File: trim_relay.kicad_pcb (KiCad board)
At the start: 2 copper layers, 75 x 71 mm, 46 parts, among them J1 Conn_01x01, J10 Conn_01x01, J11 Conn_01x01, J12 Conn_01x01, J2 Conn_01x01, J3 Conn_01x01, J4 Conn_01x01, J5 Conn_01x01, J6 Conn_01x01, J7 Conn_01x01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

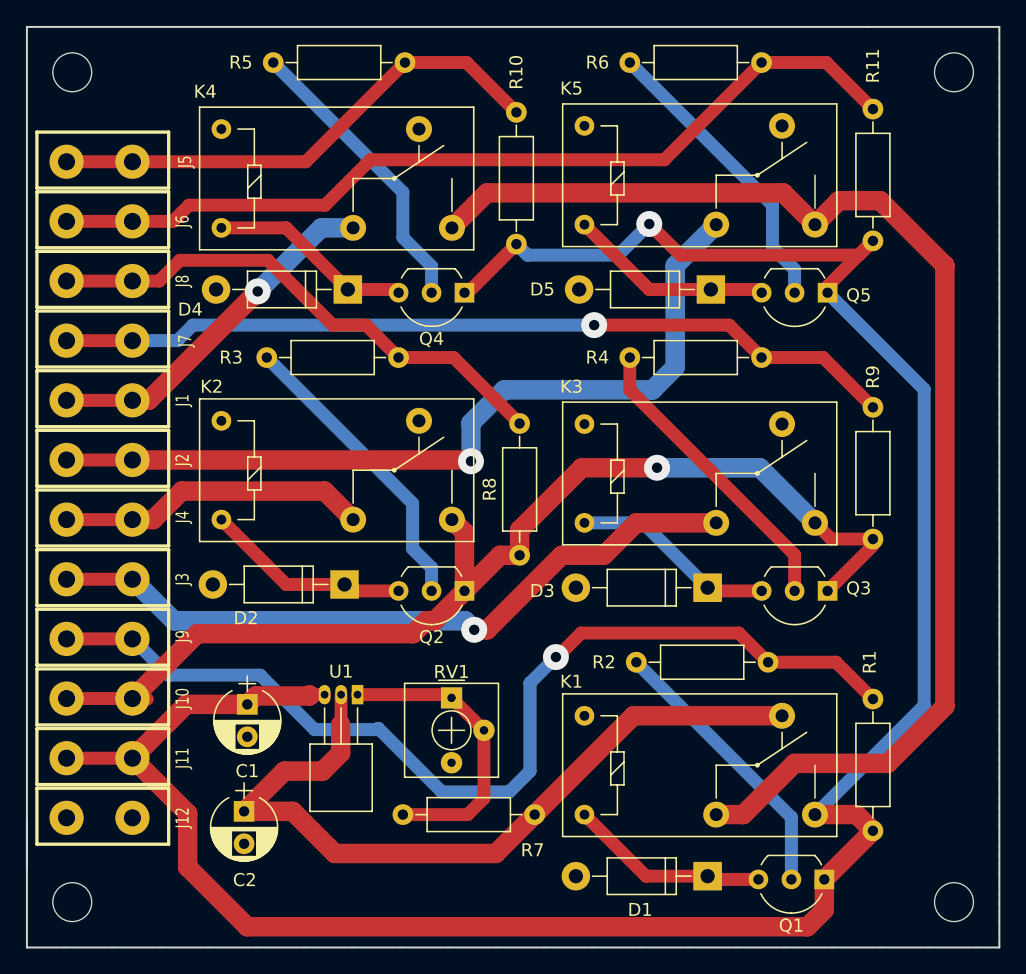
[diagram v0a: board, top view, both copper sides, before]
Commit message: Redid schematic and pcb, removed transistors
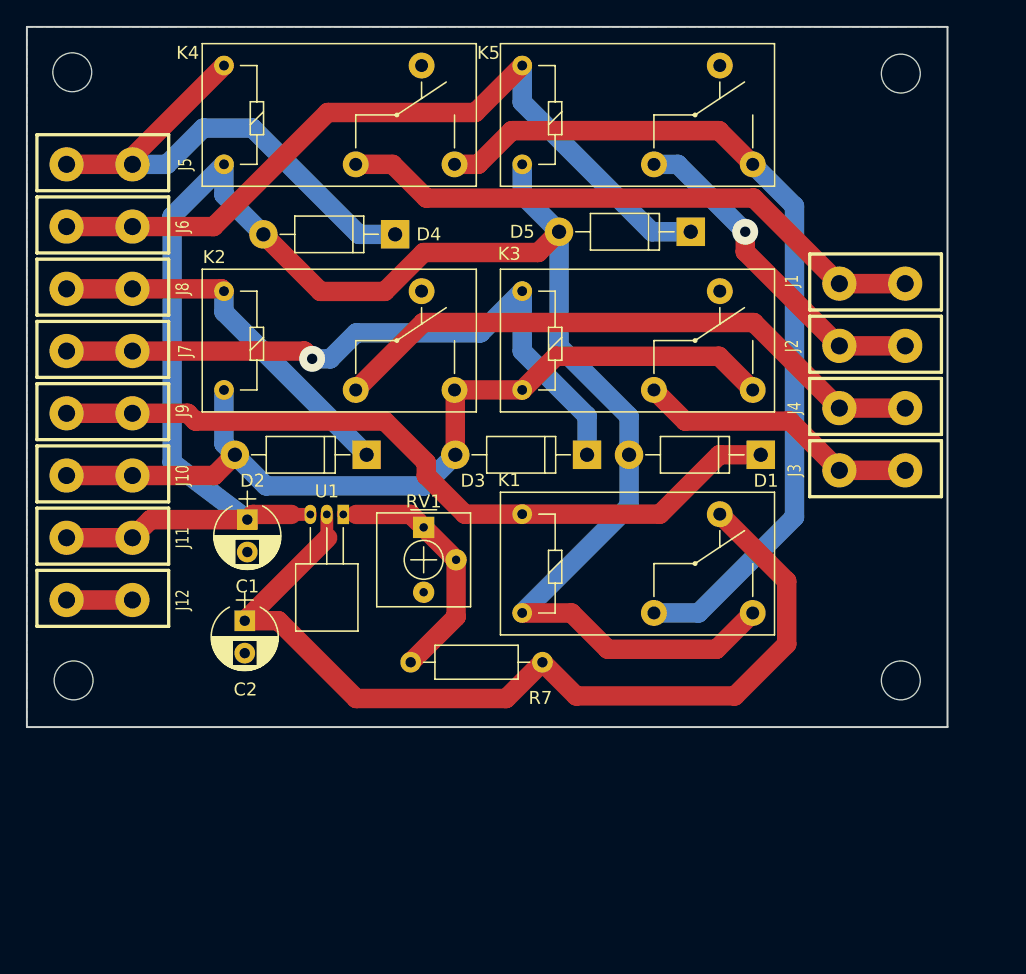
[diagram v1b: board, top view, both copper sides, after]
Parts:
- removed Q1, Q2, Q3, Q4, Q5: 2N3906, TO_SOT_Packages_THT:TO-92_Inline_Wide
- removed R1, R10, R11, R8, R9: 10K, Resistors_THT:R_Axial_DIN0207_L6.3mm_D2.5mm_P10.16mm_Horizontal
- removed R2, R3, R4, R5, R6: 3K9, Resistors_THT:R_Axial_DIN0207_L6.3mm_D2.5mm_P10.16mm_Horizontal
- moved J1 60.3 mm to (105.2, 59.8)
- moved J2 60.2 mm to (105.2, 64.6)
- moved J4 60.2 mm to (105.2, 69.4)
- moved J3 60.2 mm to (105.2, 74.2)
- moved D1 32.8 mm to (96.6, 73.0)
- moved REF** 17.6 mm to (107.4, 90.4)
- moved J9 17.4 mm to (45.6, 69.8)
- moved J10 17.2 mm to (45.6, 74.6)
- moved REF** 17.1 mm to (43.6, 90.4)
- moved J11 17.0 mm to (45.6, 79.4)
- moved J12 16.8 mm to (45.6, 84.2)
- moved K1 16.3 mm to (78.2, 85.2)
- moved C2 14.7 mm to (56.8, 85.8)
- moved C1 14.2 mm to (57.0, 78.0)
- moved U1 13.9 mm to (64.4, 77.6)
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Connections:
- D1 pad 1: Net-(D1-Pad1) -> FLAP_DN
- D1 pad 2: GND -> VDD
- D2 pad 1: Net-(D2-Pad1) -> TRIM_AL_UP_IN
- D2 pad 2: GND -> VCC
- D3 pad 1: Net-(D3-Pad1) -> TRIM_AL_DN_IN
- D3 pad 2: GND -> VCC
- D4 pad 1: Net-(D4-Pad1) -> TRIM_ELEV_UP_IN
- D4 pad 2: GND -> VDD
- D5 pad 1: Net-(D5-Pad1) -> TRIM_ELEV_DN_IN
- D5 pad 2: GND -> VDD
- K1 pad 1: Net-(D1-Pad1) -> VDD
- K1 pad 5: GND -> FLAP_DN
- K2 pad 1: Net-(D2-Pad1) -> VCC
- K2 pad 5: GND -> TRIM_AL_UP_IN
- K3 pad 1: Net-(D3-Pad1) -> VCC
- K3 pad 5: GND -> TRIM_AL_DN_IN
- K4 pad 1: Net-(D4-Pad1) -> VDD
- K4 pad 5: GND -> TRIM_ELEV_UP_IN
- K5 pad 1: Net-(D5-Pad1) -> VDD
- K5 pad 5: GND -> TRIM_ELEV_DN_IN
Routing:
- net TRIM_AL_DN_OUT: track 99.0 -> 21.9 mm, vias 1 -> 0
- net TRIM_ELEV_DN_OUT: track 78.8 -> 26.1 mm
- net VDD: track 189.6 -> 146.2 mm, vias 1 -> 0
- net V_ADJ: track 104.5 -> 71.2 mm
- net V_ELEV: track 98.1 -> 67.6 mm
- net Net-(Q3-Pad2): track 23.3 -> 0.00 mm
- net Net-(Q2-Pad2): track 23.3 -> 0.00 mm
- net Net-(Q5-Pad2): track 23.0 -> 0.00 mm
- net Net-(Q4-Pad2): track 22.8 -> 0.00 mm
- net Net-(Q1-Pad2): track 21.7 -> 0.00 mm
- net FLAP_DN: track 78.6 -> 59.2 mm, vias 1 -> 0
- net TRIM_ELEV_UP_OUT: track 27.6 -> 46.2 mm, vias 1 -> 0
- net VCC: track 86.1 -> 68.2 mm, vias 1 -> 0
- net Net-(D2-Pad1): track 15.9 -> 0.00 mm
- net Net-(D5-Pad1): track 15.8 -> 0.00 mm
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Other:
- board size 75 x 71 mm -> 71 x 54 mm

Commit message: Added solder bridges, redid routing
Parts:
- added J13: GS2, Connectors:GS2, F.Cu at (102.4, 81.6)
- added J14: GS2, Connectors:GS2, F.Cu at (106.6, 81.6)
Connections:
- K1 pad 4: V_ADJ -> V_ELEV_INPUT
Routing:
- net V_ELEV: track 67.6 -> 84.0 mm, vias 0 -> 1
- net VDD: track 146.2 -> 160.4 mm, vias 0 -> 1
- net V_ELEV_INPUT: track 0.00 -> 11.2 mm
- net V_ADJ: track 71.2 -> 66.9 mm
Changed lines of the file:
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@@
 (kicad_pcb (version 4) (host pcbnew 4.0.7-e2-6376~61~ubuntu18.04.1)
   (general
-    (links 56)
+    (links 59)
     (no_connects 0)
-    (area 22.642858 38.525 125.585715 95.475)
+    (area 39.924999 39.924999 111.075001 94.075001)
     (thickness 1.6)
     (drawings 17)
-    (tracks 130)
+    (tracks 143)
     (zones 0)
-    (modules 31)
-    (nets 16)
+    (modules 33)
+    (nets 17)
   )
   (page USLetter)
@@
   (net 14 VDD)
   (net 15 VCC)
+  (net 16 V_ELEV_INPUT)
   (net_class Default "This is the default net class."
     (clearance 0.2)
@@
     (add_net V_ADJ)
     (add_net V_ELEV)
+    (add_net V_ELEV_INPUT)
   )
   (module Relays_THT:Relay_SPDT_OMRON-G5Q (layer F.Cu)
@@
       (net 14 VDD))
     (pad 4 thru_hole circle (at 15.24 -7.62 180) (size 2 2) (drill 1) (layers *.Cu *.Mask)
-      (net 3 V_ADJ))
+      (net 16 V_ELEV_INPUT))
     (pad 5 thru_hole circle (at 0 -7.62 180) (size 1.52 1.52) (drill 0.76) (layers *.Cu *.Mask)
       (net 8 FLAP_DN))
@@
       (net 1 GND) (solder_mask_margin 0.0762) (clearance 0.254))
   )
+  (module Connectors:GS2 (layer F.Cu)
+    (at 102.4 81.6)
+    (descr "2-pin solder bridge")
+    (tags "solder bridge")
+    (attr smd)
+    (fp_text reference J13 (at 1.78 0 90) (layer F.SilkS)
+      (effects (font (size 1 1) (thickness 0.15)))
+    )
+    (fp_text value GS2 (at -1.8 0 90) (layer F.Fab)
+      (effects (font (size 1 1) (thickness 0.15)))
+    )
+    (fp_line (start 1.1 -1.45) (end 1.1 1.5) (layer F.CrtYd) (width 0.05))
+    (fp_line (start 1.1 1.5) (end -1.1 1.5) (layer F.CrtYd) (width 0.05))
+    (fp_line (start -1.1 1.5) (end -1.1 -1.45) (layer F.CrtYd) (width 0.05))
+    (fp_line (start -1.1 -1.45) (end 1.1 -1.45) (layer F.CrtYd) (width 0.05))
+    (fp_line (start -0.89 -1.27) (end -0.89 1.27) (layer F.SilkS) (width 0.12))
+    (fp_line (start 0.89 1.27) (end 0.89 -1.27) (layer F.SilkS) (width 0.12))
+    (fp_line (start 0.89 1.27) (end -0.89 1.27) (layer F.SilkS) (width 0.12))
+    (fp_line (start -0.89 -1.27) (end 0.89 -1.27) (layer F.SilkS) (width 0.12))
+    (pad 1 smd rect (at 0 -0.64) (size 1.27 0.97) (layers F.Cu F.Paste F.Mask)
+      (net 16 V_ELEV_INPUT))
+    (pad 2 smd rect (at 0 0.64) (size 1.27 0.97) (layers F.Cu F.Paste F.Mask)
+      (net 3 V_ADJ))
+  )
+  (module Connectors:GS2 (layer F.Cu)
+    (at 106.6 81.6)
+    (descr "2-pin solder bridge")
+    (tags "solder bridge")
+    (attr smd)
+    (fp_text reference J14 (at 1.78 0 90) (layer F.SilkS)
+      (effects (font (size 1 1) (thickness 0.15)))
+    )
+    (fp_text value GS2 (at -1.8 0 90) (layer F.Fab)
+      (effects (font (size 1 1) (thickness 0.15)))
+    )
+    (fp_line (start 1.1 -1.45) (end 1.1 1.5) (layer F.CrtYd) (width 0.05))
+    (fp_line (start 1.1 1.5) (end -1.1 1.5) (layer F.CrtYd) (width 0.05))
+    (fp_line (start -1.1 1.5) (end -1.1 -1.45) (layer F.CrtYd) (width 0.05))
+    (fp_line (start -1.1 -1.45) (end 1.1 -1.45) (layer F.CrtYd) (width 0.05))
+    (fp_line (start -0.89 -1.27) (end -0.89 1.27) (layer F.SilkS) (width 0.12))
+    (fp_line (start 0.89 1.27) (end 0.89 -1.27) (layer F.SilkS) (width 0.12))
+    (fp_line (start 0.89 1.27) (end -0.89 1.27) (layer F.SilkS) (width 0.12))
+    (fp_line (start -0.89 -1.27) (end 0.89 -1.27) (layer F.SilkS) (width 0.12))
+    (pad 1 smd rect (at 0 -0.64) (size 1.27 0.97) (layers F.Cu F.Paste F.Mask)
+      (net 2 V_ELEV))
+    (pad 2 smd rect (at 0 0.64) (size 1.27 0.97) (layers F.Cu F.Paste F.Mask)
+      (net 14 VDD))
+  )
   (gr_line (start 111 94) (end 40 94) (angle 90) (layer Edge.Cuts) (width 0.15))
   (gr_line (start 40 40) (end 111 40) (angle 90) (layer Edge.Cuts) (width 0.15))
@@
   )
   (segment (start 43.06 84.2) (end 48.14 84.2) (width 1.5) (layer F.Cu) (net 1) (status 30))
+  (segment (start 106.6 78.8) (end 105.6 77.8) (width 1.5) (layer B.Cu) (net 2))
+  (segment (start 105.6 77.8) (end 99.2 77.8) (width 1.5) (layer B.Cu) (net 2))
+  (segment (start 106.6 80.96) (end 106.6 78.8) (width 1) (layer F.Cu) (net 2) (status 10))
+  (via (at 106.6 78.8) (size 2) (drill 0.8) (layers F.Cu B.Cu) (net 2))
+  (segment (start 105.6 77.8) (end 99.2 77.8) (width 1) (layer B.Cu) (net 2))
   (segment (start 95.98 50.6) (end 99.2 53.82) (width 1.5) (layer B.Cu) (net 2) (status 10))
   (segment (start 91.8 85.2) (end 88.36 85.2) (width 1.5) (layer B.Cu) (net 2) (status 20))
@@
   (segment (start 77.4 48) (end 93.38 48) (width 1.5) (layer F.Cu) (net 2))
   (segment (start 74.8 50.6) (end 77.4 48) (width 1.5) (layer F.Cu) (net 2))
-  (segment (start 93.44 77.58) (end 98.6 82.74) (width 1.5) (layer F.Cu) (net 3) (status 400010))
-  (segment (start 82.36 91.6) (end 79.76 89) (width 1.5) (layer F.Cu) (net 3) (status 800020))
-  (segment (start 94.6 91.6) (end 82.36 91.6) (width 1.5) (layer F.Cu) (net 3))
-  (segment (start 98.6 87.6) (end 94.6 91.6) (width 1.5) (layer F.Cu) (net 3))
-  (segment (start 98.6 82.74) (end 98.6 87.6) (width 1.5) (layer F.Cu) (net 3))
+  (segment (start 102.4 82.24) (end 102.4 83) (width 1) (layer F.Cu) (net 3) (status 10))
+  (segment (start 81.36 90.6) (end 98.6 90.6) (width 1.5) (layer F.Cu) (net 3))
+  (segment (start 98.6 90.6) (end 102.4 86.8) (width 1.5) (layer F.Cu) (net 3))
+  (segment (start 102.4 86.8) (end 102.4 83) (width 1.5) (layer F.Cu) (net 3))
+  (segment (start 81.36 90.6) (end 79.76 89) (width 1.5) (layer F.Cu) (net 3) (status 20))
   (segment (start 56.8 85.8) (end 59.4 85.8) (width 1.5) (layer F.Cu) (net 3) (status 10))
   (segment (start 76.96 91.8) (end 79.76 89) (width 1.5) (layer F.Cu) (net 3) (status 20))
@@
   (segment (start 70.6 78.6) (end 69.6 77.6) (width 1.5) (layer F.Cu) (net 13) (status 10))
   (segment (start 69.6 77.6) (end 65.4 77.6) (width 1.5) (layer F.Cu) (net 13))
-  (segment (start 78.2 85.2) (end 82 85.2) (width 1.5) (layer F.Cu) (net 14) (status 400010))
-  (segment (start 93.18 88) (end 95.98 85.2) (width 1.5) (layer F.Cu) (net 14) (status 800020))
+  (segment (start 95.98 85.2) (end 105.8 85.2) (width 1.5) (layer B.Cu) (net 14) (status 10))
+  (segment (start 105.8 85.2) (end 106.6 84.4) (width 1.5) (layer B.Cu) (net 14))
+  (segment (start 106.6 82.24) (end 106.6 84.4) (width 1) (layer F.Cu) (net 14) (status 10))
+  (segment (start 106.6 84.4) (end 105.8 85.2) (width 1) (layer B.Cu) (net 14))
+  (via (at 106.6 84.4) (size 2) (drill 0.8) (layers F.Cu B.Cu) (net 14))
+  (segment (start 78.2 85.2) (end 82 85.2) (width 1.5) (layer F.Cu) (net 14) (status 10))
+  (segment (start 93.18 88) (end 95.98 85.2) (width 1.5) (layer F.Cu) (net 14) (status 20))
   (segment (start 84.8 88) (end 93.18 88) (width 1.5) (layer F.Cu) (net 14))
   (segment (start 82 85.2) (end 84.8 88) (width 1.5) (layer F.Cu) (net 14))
@@
   (segment (start 48.14 74.6) (end 54.44 74.6) (width 1.5) (layer F.Cu) (net 15) (status 10))
   (segment (start 54.44 74.6) (end 56.04 73) (width 1.5) (layer F.Cu) (net 15) (status 20))
+  (segment (start 102.4 80.96) (end 102.4 79.6) (width 1) (layer F.Cu) (net 16) (status 10))
+  (segment (start 100.38 77.58) (end 102.4 79.6) (width 1.5) (layer F.Cu) (net 16))
+  (segment (start 100.38 77.58) (end 93.44 77.58) (width 1.5) (layer F.Cu) (net 16) (status 20))
   (zone (net 1) (net_name GND) (layer B.Cu) (hatch edge 0.508)
     (connect_pads (clearance 0.508))

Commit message: Final version
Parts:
- U1: footprint TO_SOT_Packages_THT:TO-92_Horizontal2_Inline_Narrow_Oval -> TO_SOT_Packages_THT:TO-220-3_Horizontal
- moved RV1 32.2 mm to (99.6, 92.6), turned to 180 degrees
- moved R7 24.1 mm to (93.6, 90.6), turned to 180 degrees
- moved U1 15.5 mm to (73.2, 90.4), turned to 90 degrees
- moved C2 10.4 mm to (63.8, 78.1)
- moved K1 0.70 mm to (78.2, 84.5)
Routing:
- net VDD: track 160.4 -> 178.4 mm
- net V_ADJ: track 66.9 -> 55.2 mm, vias 0 -> 1
- net Net-(R7-Pad1): track 19.5 -> 29.9 mm
- net FLAP_DN: track 59.2 -> 58.7 mm
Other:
- rule pad_to_mask_clearance: 0.2 -> 0.0508

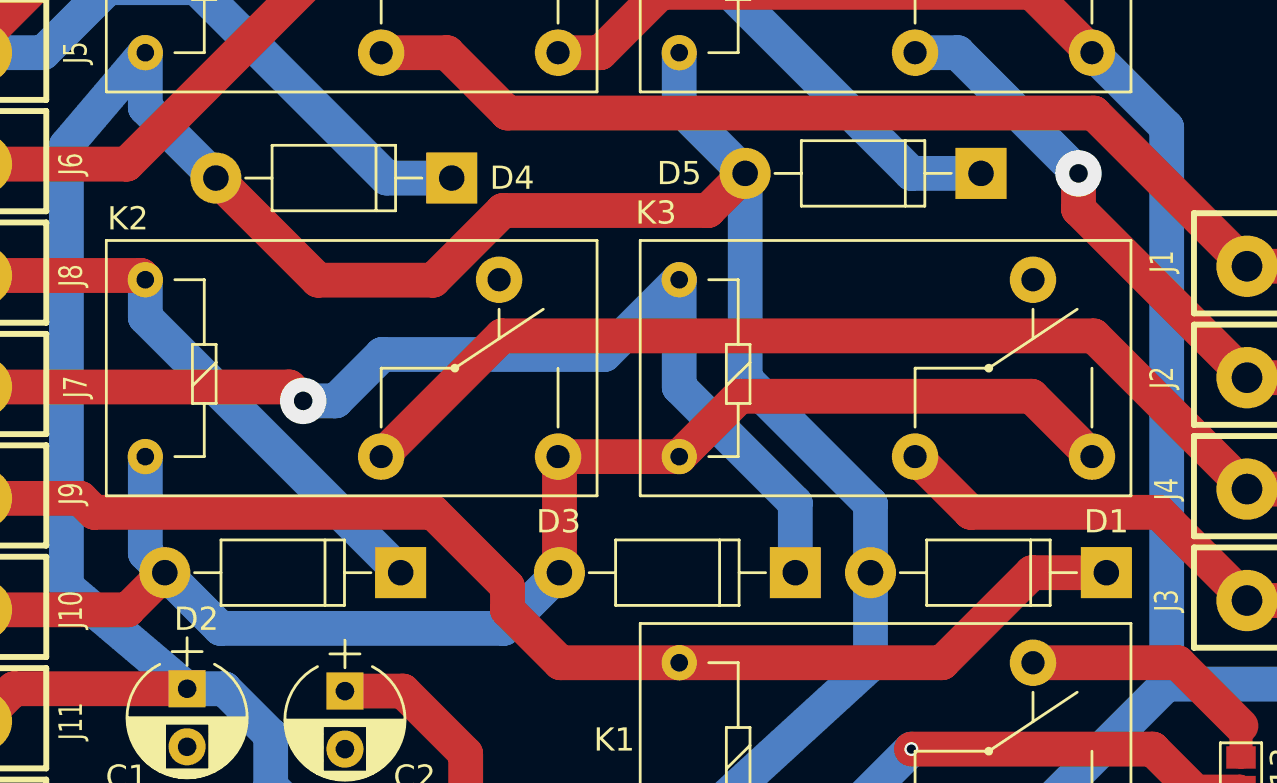
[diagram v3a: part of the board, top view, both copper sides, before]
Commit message: Diodes were backwards
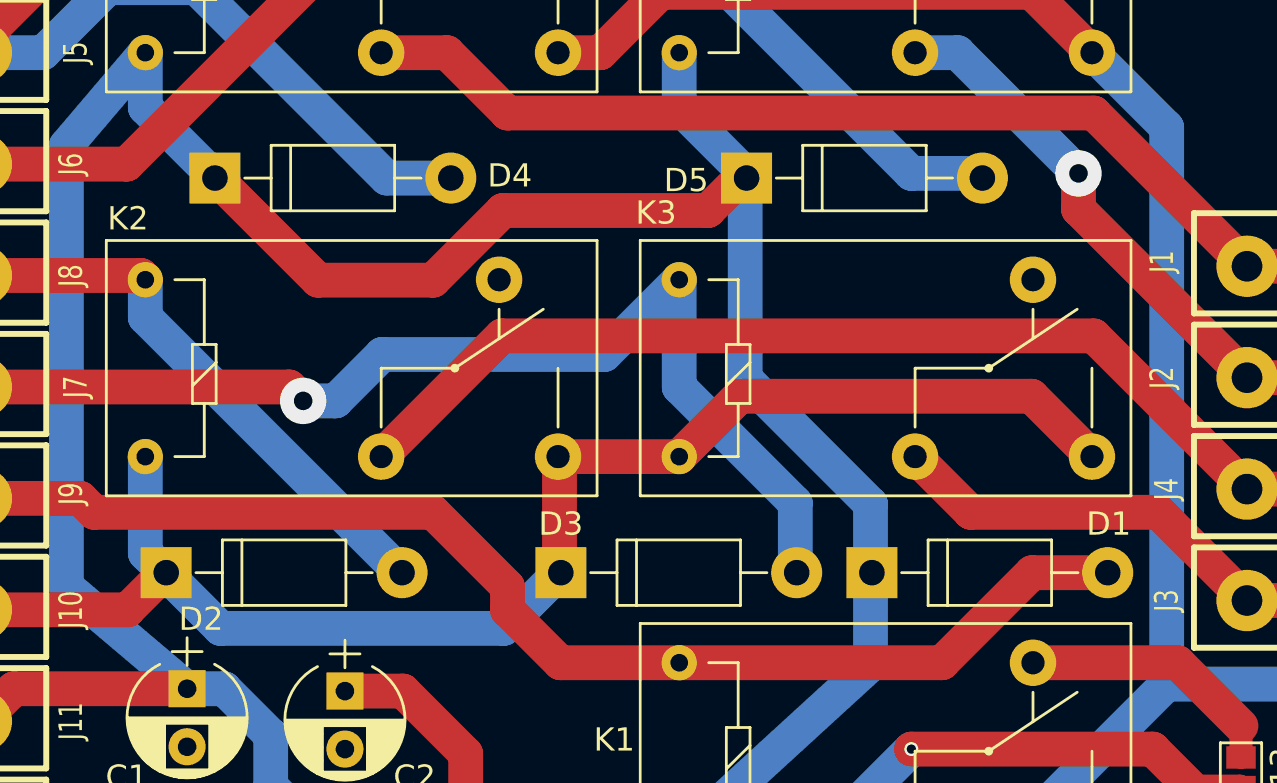
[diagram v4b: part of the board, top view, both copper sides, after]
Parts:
- moved D4 10.2 mm to (58.2, 56.0), turned to 0 degrees
- moved D5 10.1 mm to (81.1, 56.0), turned to 0 degrees
- moved D3 10.1 mm to (73.1, 73.0), turned to 0 degrees
- moved D2 10.1 mm to (56.1, 73.0), turned to 0 degrees
- moved D1 10.1 mm to (86.5, 73.0), turned to 0 degrees
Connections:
- D1 pad 1: FLAP_DN -> VDD
- D1 pad 2: VDD -> FLAP_DN
- D2 pad 1: TRIM_AL_UP_IN -> VCC
- D2 pad 2: VCC -> TRIM_AL_UP_IN
- D3 pad 1: TRIM_AL_DN_IN -> VCC
- D3 pad 2: VCC -> TRIM_AL_DN_IN
- D4 pad 1: TRIM_ELEV_UP_IN -> VDD
- D4 pad 2: VDD -> TRIM_ELEV_UP_IN
- D5 pad 1: TRIM_ELEV_DN_IN -> VDD
- D5 pad 2: VDD -> TRIM_ELEV_DN_IN
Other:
- board text added: "www-bit-builder.com-trim_relay-v1.1"
- board text removed: "www-bit-builder.com-trim_relay-v1.0"
